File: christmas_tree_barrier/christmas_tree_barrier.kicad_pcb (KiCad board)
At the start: 2 copper layers, 15 parts, among them CON1 AVR-ISP-6, IC1 MIC5225-3.3, J1 USB_OTG, J2 JSTPH, J3 JSTPH, Q1 PN2222A, U1 ATTINY45-20SU, Y1 8Mhz

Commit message: Working on new pcb
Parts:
- J2, J3: moved to B.Cu
- Q1: value PN2222A -> Q_PNP_BEC
- moved Y1 26.6 mm to (151.4, 115.6)
- moved J1 26.3 mm to (159.8, 130.7)
- moved R1 25.4 mm to (143.3, 105.4)
- moved J3 17.9 mm to (165.1, 105.0), turned to 90 degrees
- moved Q1 10.8 mm to (163.8, 115.6), turned to 90 degrees
- moved U1 9.94 mm to (135.9, 105.4)
- moved CON1 8.78 mm to (134.6, 116.8)
- moved D2 7.33 mm to (135.9, 128.3)
- moved IC1 7.20 mm to (160.0, 123.2), turned to 90 degrees
- moved J2 3.73 mm to (153.8, 105.0), turned to 270 degrees
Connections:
- Q1 pad 1: GND -> Net-(Q1-Pad1)
- Q1 pad 2: Net-(Q1-Pad2) -> GND
- R2 pad 2: Net-(Q1-Pad2) -> Net-(Q1-Pad1)

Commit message: Place parts nicely
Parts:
- moved D2 36.9 mm to (172.7, 129.7), turned to 270 degrees
- moved D1 29.6 mm to (147.3, 129.5), turned to 270 degrees
- moved R1 27.0 mm to (152.4, 130.8), turned to 180 degrees
- moved U1 23.9 mm to (157.5, 115.6), turned to 270 degrees
- moved C1 19.5 mm to (165.1, 124.5)
- moved CON1 12.8 mm to (147.3, 115.6)
- moved Y1 12.4 mm to (160.0, 106.7), turned to 180 degrees
- moved C2 12.1 mm to (165.1, 114.3)
- moved Q1 9.67 mm to (172.7, 119.4), turned to 270 degrees
- moved R3 7.26 mm to (167.6, 130.8)
- moved J3 6.50 mm to (171.6, 105.0)
- moved R2 6.35 mm to (165.1, 118.1)
- moved J2 5.08 mm to (148.7, 105.1)
- moved J1 0.70 mm to (159.8, 130.0)

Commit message: Mostly finalize placement and outline
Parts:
- added REF**: MountingHole_2.2mm_M2, Mounting_Holes:MountingHole_2.2mm_M2, F.Cu at (160.0, 106.7)
- CON1: moved to B.Cu
- Q1: footprint TO_SOT_Packages_SMD:SOT-23 -> TO_SOT_Packages_SMD:SOT-23_Handsoldering
- Y1: footprint Crystals:Resonator_SMD-3pin_7.2x3.0mm_HandSoldering -> kicad-libs:Resonator_SMD_muRata_CSTCE_G-3pin_3.0x0.7mm
- moved CON1 8.89 mm to (147.3, 124.5)
- moved Y1 7.09 mm to (153.2, 108.7)
- moved J3 6.76 mm to (171.4, 111.8)
- moved J2 6.62 mm to (148.7, 111.8)
- moved Q1 2.31 mm to (172.7, 121.7)
- moved D2 1.27 mm to (171.4, 129.7)
- moved R3 1.27 mm to (167.6, 129.5), turned to 270 degrees
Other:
- board outline added: 31 x 30.5 mm

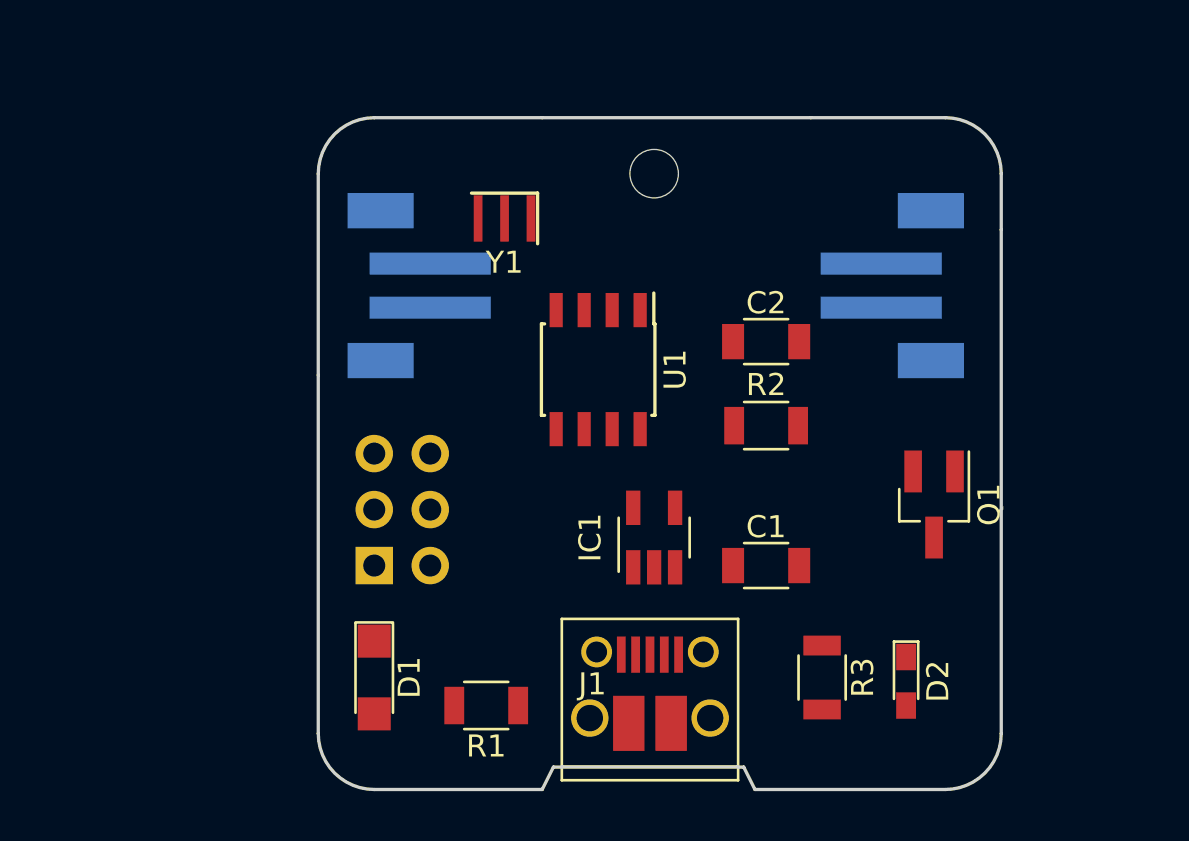
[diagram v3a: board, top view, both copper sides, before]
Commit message: Finished layout and routing Also just a bit of silkscreen
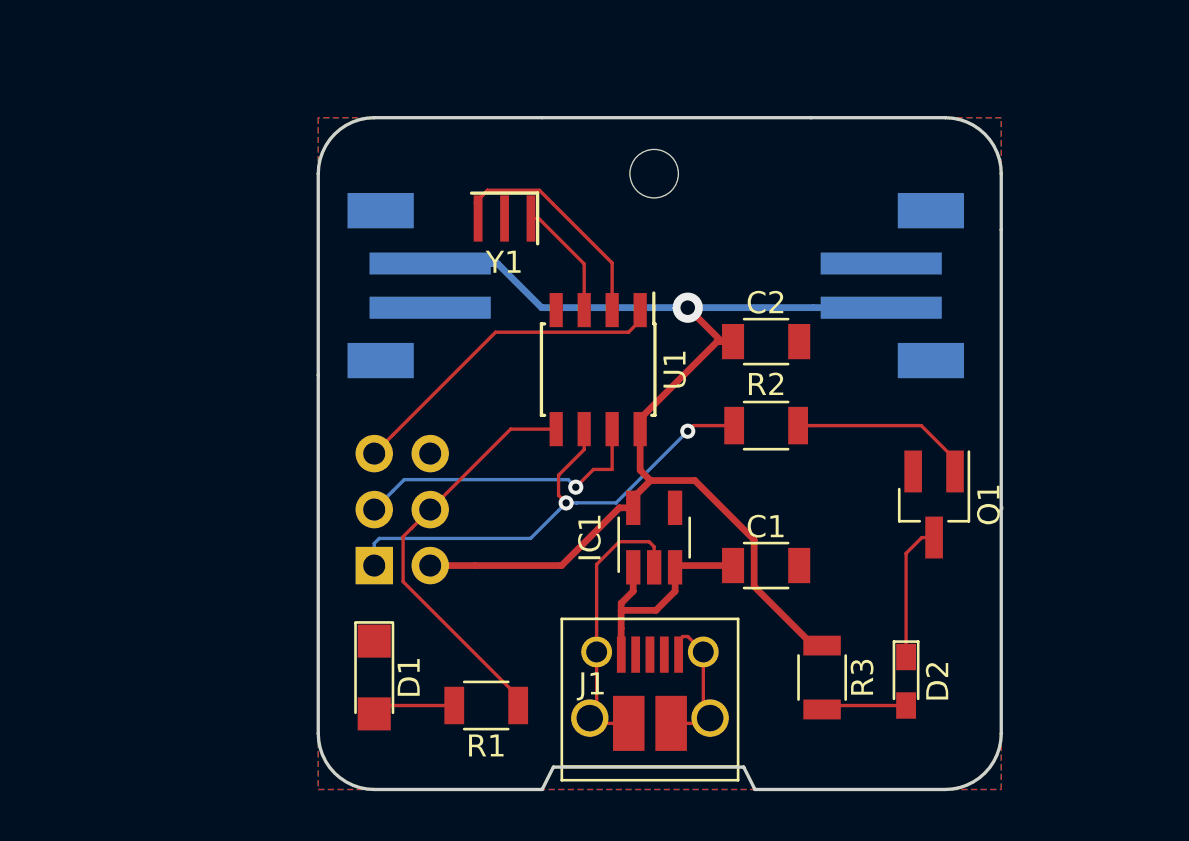
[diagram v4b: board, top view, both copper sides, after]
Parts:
- added G***: LOGO, kicad-libs:petezah-logo-tiny, B.Cu at (169.2, 125.5)
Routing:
- net +3V3: track 0.00 -> 56.6 mm, vias 0 -> 1
- net /MISO/IR: track 0.00 -> 23.5 mm, vias 0 -> 2
- net GND: track 0.00 -> 20.1 mm
- net /MOSI/INDICATOR: track 0.00 -> 18.8 mm
- net /RST: track 0.00 -> 15.0 mm
- net /SCK: track 0.00 -> 13.7 mm, vias 0 -> 1
- net Net-(U1-Pad2): track 0.00 -> 11.4 mm
- net VBUS: track 0.00 -> 10.0 mm
- net Net-(Q1-Pad1): track 0.00 -> 8.30 mm
- net Net-(D2-Pad1): track 0.00 -> 6.27 mm
- net Net-(U1-Pad3): track 0.00 -> 5.36 mm
- net Net-(D2-Pad2): track 0.00 -> 3.88 mm
- net Net-(D1-Pad2): track 0.00 -> 3.79 mm
- added copper zone on B.Cu, net GND
- added copper zone on F.Cu, net GND
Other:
- net class 3V3 added: clearance 0.3048, trace_width 0.3048, via_dia 1.3716, via_drill 0.6604
- net class Default: clearance 0.2 -> 0.1524; trace_width 0.25 -> 0.1524; via_dia 0.6 -> 0.6858; via_drill 0.4 -> 0.3302
- rule trace_clearance: 0.2 -> 0.1524
- rule trace_min: 0.2 -> 0.1524
- rule via_min_drill: 0.3 -> 0.3302
- rule via_min_size: 0.4 -> 0.6858
- board text added: "@Petezah"
- board text added: "Roomba Christmas Tree Barrier (C) Copyright 2017 Peter Dunshee @Petezah"

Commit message: Archive symbols and footprints
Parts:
- C1, C2: footprint Capacitors_SMD:C_1206 -> lib_fp:C_1206
- CON1: footprint Pin_Headers:Pin_Header_Straight_2x03_Pitch2.54mm -> lib_fp:Pin_Header_Straight_2x03_Pitch2.54mm
- D1: footprint LEDs:LED_1206 -> lib_fp:LED_1206
- D2: footprint LEDs:LED_0603_HandSoldering -> lib_fp:LED_0603_HandSoldering
- IC1: footprint TO_SOT_Packages_SMD:SOT-23-5_HandSoldering -> lib_fp:SOT-23-5_HandSoldering
- J1: footprint NurseryPager-Hardware:USB_Micro-B_10103594-0001LF -> lib_fp:USB_Micro-B_10103594-0001LF
- J2, J3: footprint Connectors_JST:JST_PH_B2B-PH-SM4-TB_02x2.00mm_Straight -> lib_fp:JST_PH_B2B-PH-SM4-TB_02x2.00mm_Straight
- Q1: footprint TO_SOT_Packages_SMD:SOT-23_Handsoldering -> lib_fp:SOT-23_Handsoldering
- R1, R2, R3: footprint Resistors_SMD:R_1206 -> lib_fp:R_1206
- U1: footprint Housings_SOIC:SOIC-8_3.9x4.9mm_Pitch1.27mm -> lib_fp:SOIC-8_3.9x4.9mm_Pitch1.27mm
- Y1: footprint kicad-libs:Resonator_SMD_muRata_CSTCE_G-3pin_3.0x0.7mm -> lib_fp:Resonator_SMD_muRata_CSTCE_G-3pin_3.0x0.7mm

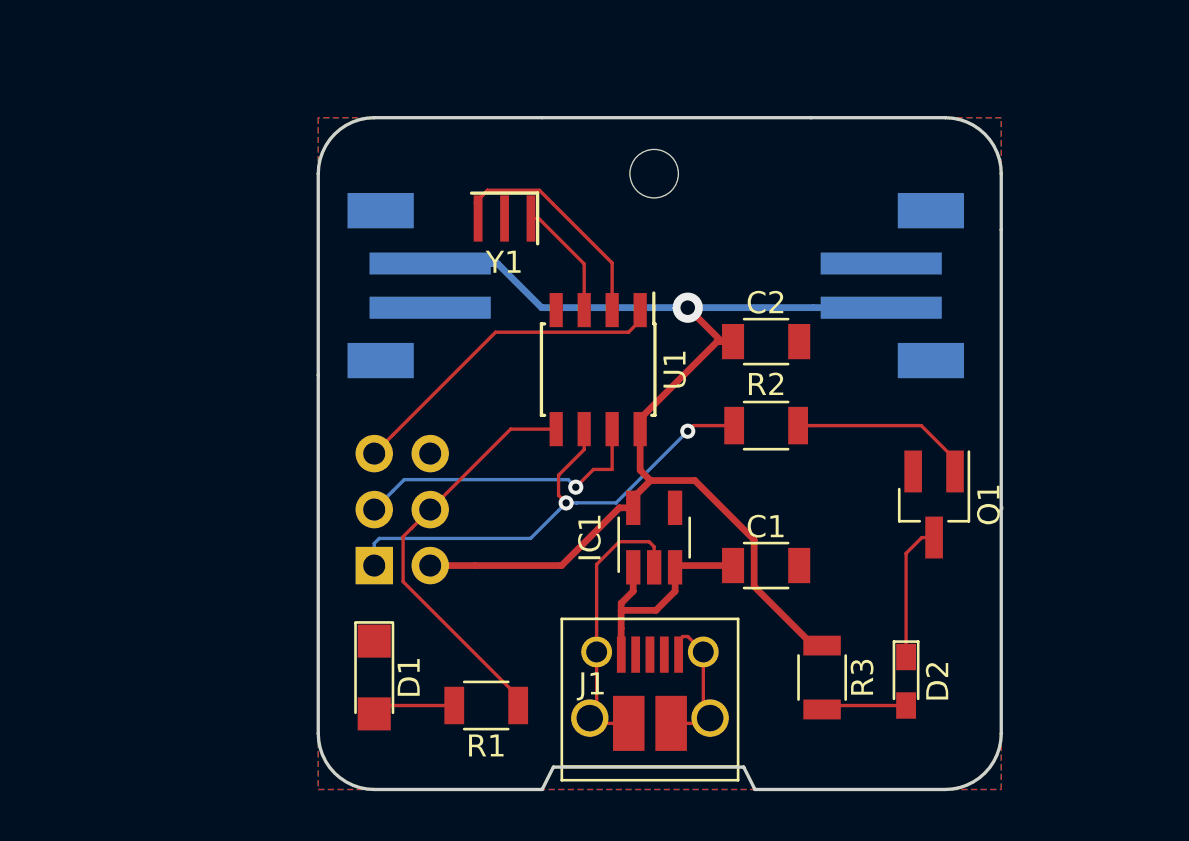
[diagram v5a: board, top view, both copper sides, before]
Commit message: Fix footprints SOIC-8 was wrong--body was too narrow and pads too short LEDs were unclear--cathode indicator was on top of solder mask area
Also plotted gerbers
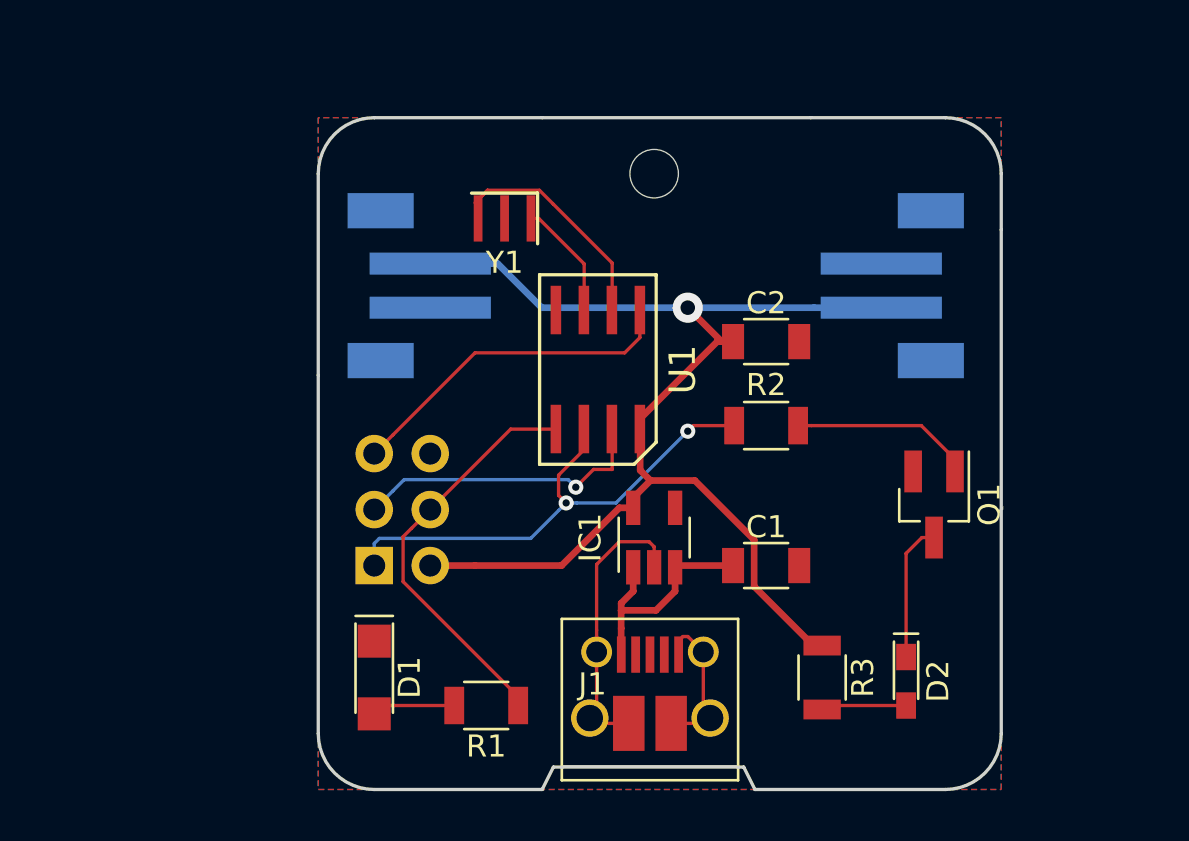
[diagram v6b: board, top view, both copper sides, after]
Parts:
- Q1: value Q_PNP_BEC -> Q_NPN_BEC
- U1: footprint lib_fp:SOIC-8_3.9x4.9mm_Pitch1.27mm -> lib_fp:SOIC-8_5.35x5.40mm_Pitch1.27mm
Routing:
- net /RST: track 15.0 -> 16.0 mm
